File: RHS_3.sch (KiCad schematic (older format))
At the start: 64 parts, among them IC1 ATMEGA328P-A, IC2 CC1101, IC3 CC1101_Chip, J1 Glass Breakage Detector, J2 ANT, P4 ISP Bottom, P5 ISP Top, P6 FTDI, P7 ISP 10, SW1 Reset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

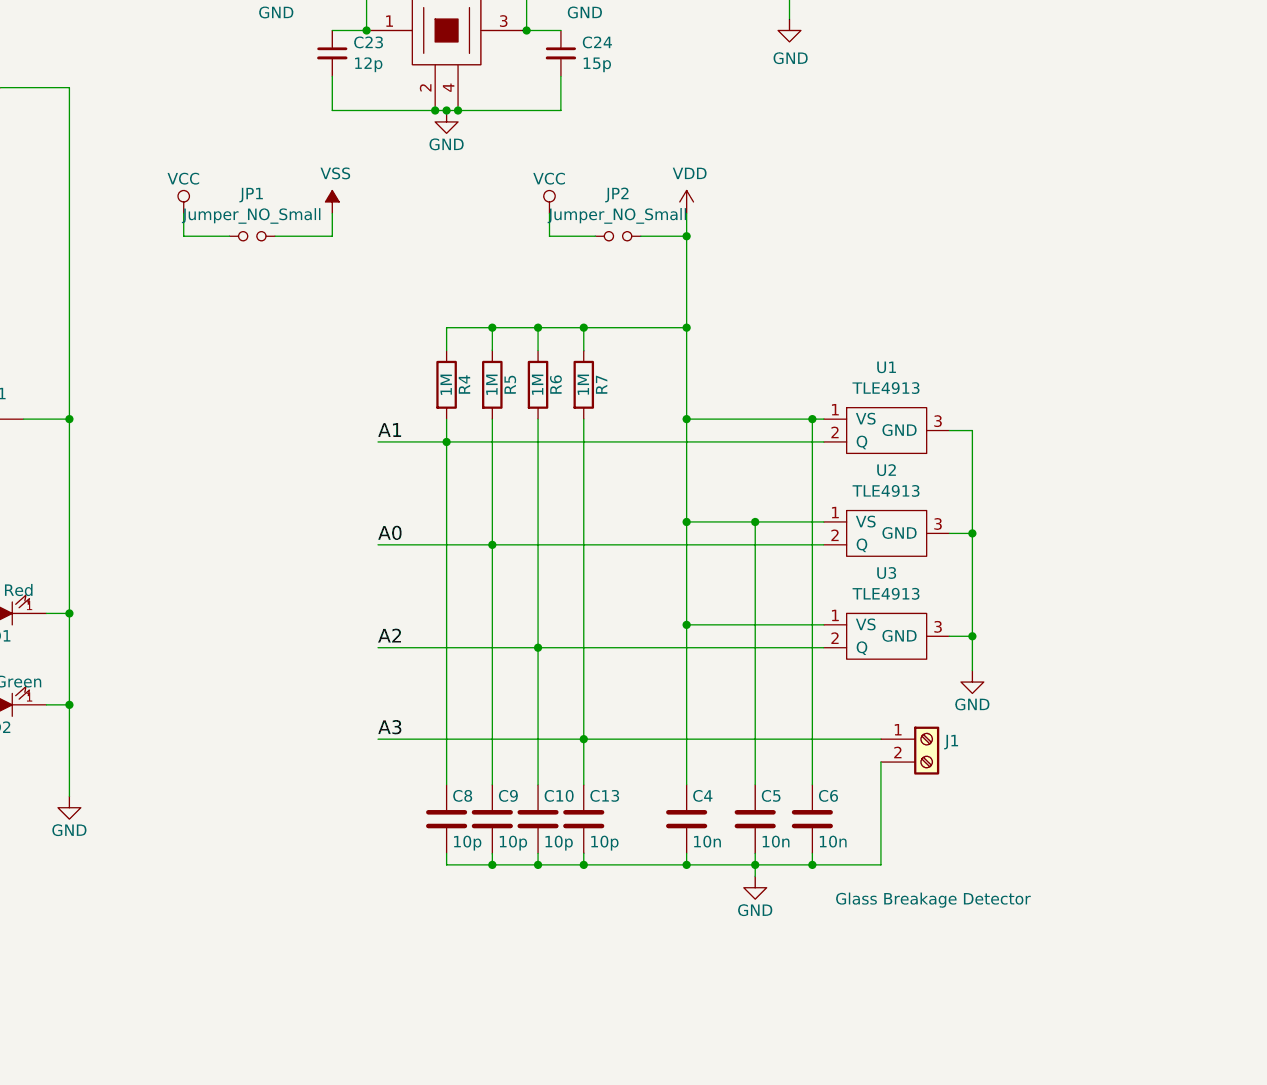
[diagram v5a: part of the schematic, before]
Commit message: layout changed
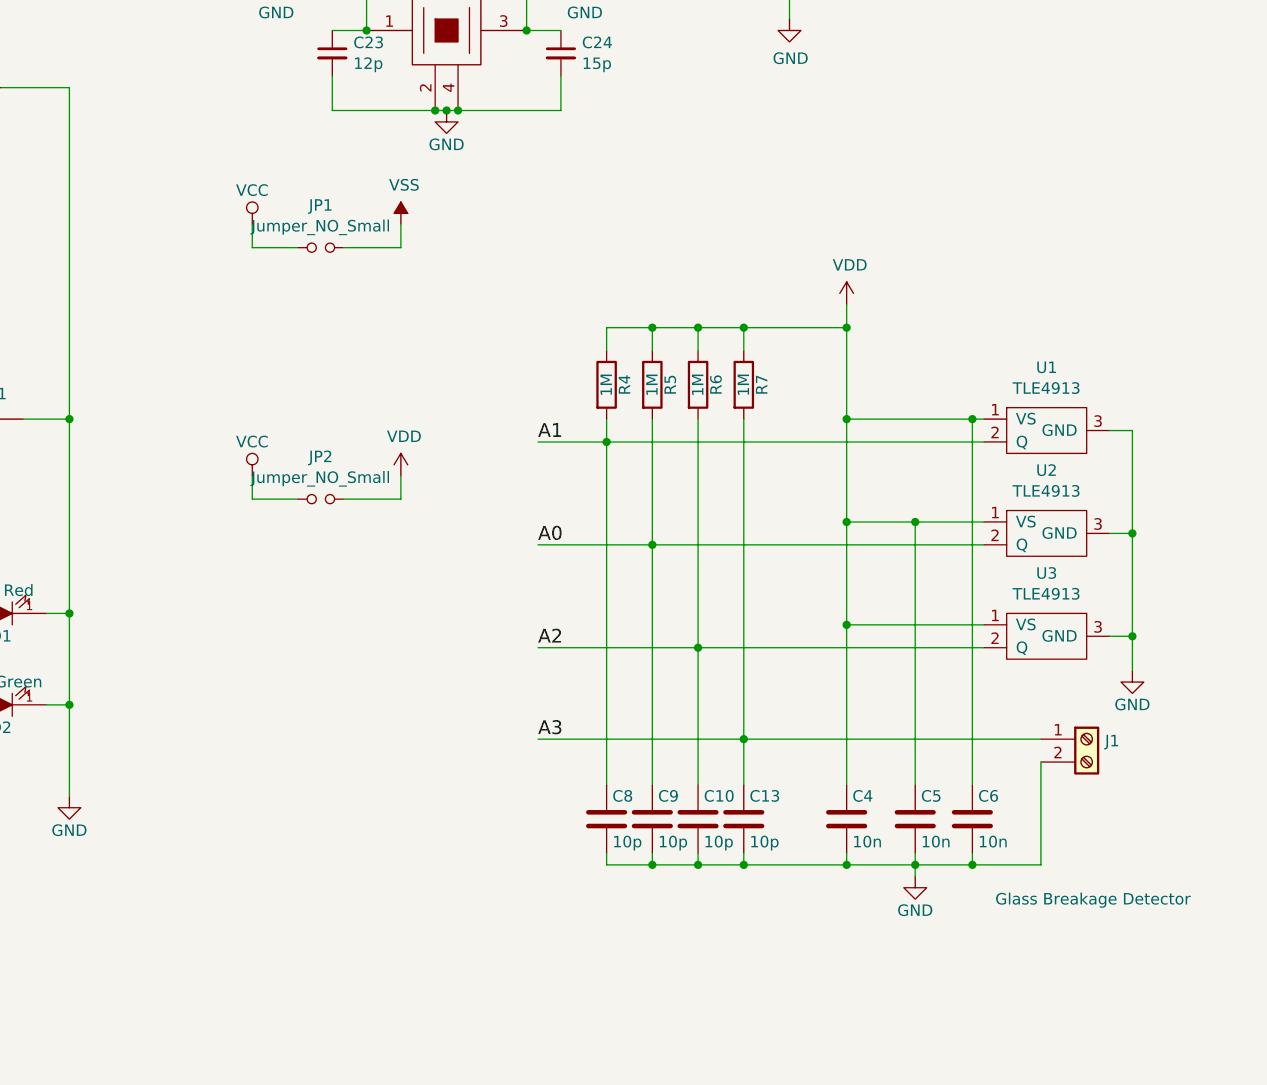
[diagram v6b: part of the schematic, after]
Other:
- moved on the sheet: C10, C13, C4, C5, C6, C8, C9, J1, JP1, JP2, R4, R5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

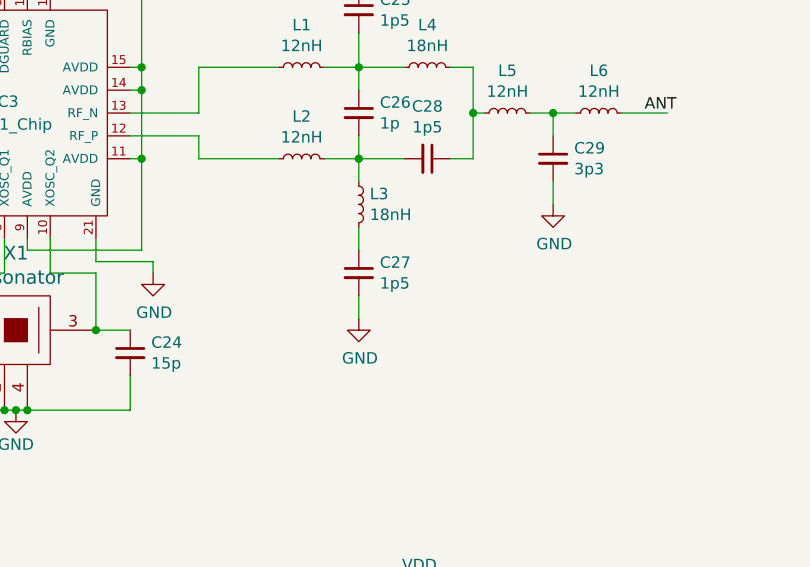
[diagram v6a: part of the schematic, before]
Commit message: part numbers added
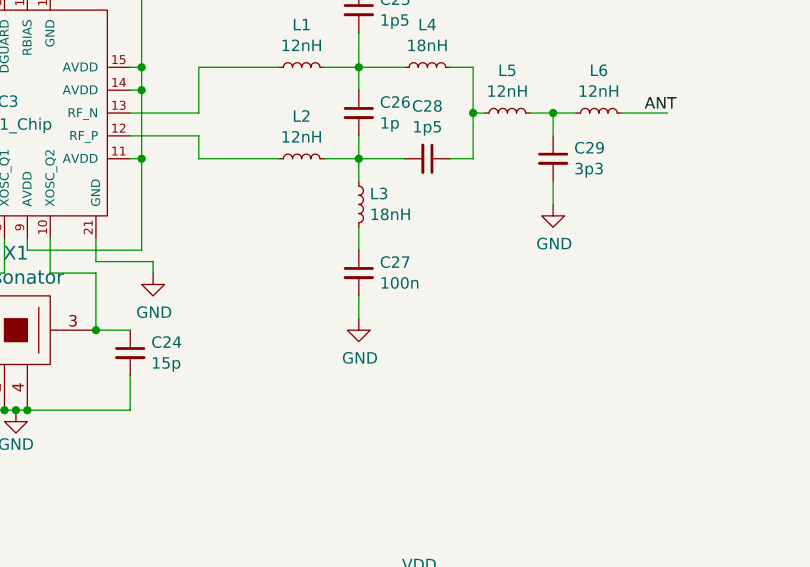
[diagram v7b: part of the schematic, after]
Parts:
- C15: LCSC Part # (none) -> C23733
- C16, C17, C18, C19, C20, C21, C22: LCSC Part # (none) -> C1525
- C23: LCSC Part # (none) -> C1547
- C24: LCSC Part # (none) -> C1548
- C25, C28: LCSC Part # (none) -> C1552
- C26: LCSC Part # (none) -> C1550
- C27: value 1p5 -> 100n; LCSC Part # (none) -> C1525
- C29: LCSC Part # (none) -> C1565
- IC3: LCSC Part # (none) -> C29953
- L1, L2, L5, L6: LCSC Part # (none) -> C24563
- L3, L4: LCSC Part # (none) -> C24562
- X1: LCSC Part # (none) -> C91747
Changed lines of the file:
@@
 F 2 "Package_DFN_QFN:QFN-20-1EP_4x4mm_P0.5mm_EP2.5x2.5mm" H 7850 1650 50  0001 C CNN
 F 3 "" H 7850 1650 50  0001 C CNN
+F 4 "C29953" H 7850 1650 50  0001 C CNN "LCSC Part #"
 	1    7850 1650
 	1    0    0    -1
@@
 F 2 "Oscillator:Oscillator_SMD_EuroQuartz_XO32-4Pin_3.2x2.5mm" H 7900 2831 60  0001 C CNN
 F 3 "" H 7900 2550 60  0000 C CNN
+F 4 "C91747" H 7900 2600 50  0001 C CNN "LCSC Part #"
 	1    7900 2600
 	1    0    0    -1
@@
 F 2 "Capacitor_SMD:C_0402_1005Metric" H 7400 2700 50  0001 C CNN
 F 3 "~" H 7400 2700 50  0001 C CNN
+F 4 "C1547" H 7400 2700 50  0001 C CNN "LCSC Part #"
 	1    7400 2700
 	1    0    0    -1
@@
 F 2 "Capacitor_SMD:C_0402_1005Metric" H 8400 2700 50  0001 C CNN
 F 3 "~" H 8400 2700 50  0001 C CNN
+F 4 "C1548" H 8400 2700 50  0001 C CNN "LCSC Part #"
 	1    8400 2700
 	1    0    0    -1
@@
 F 2 "Capacitor_SMD:C_0402_1005Metric" H 7150 2050 50  0001 C CNN
 F 3 "~" H 7150 2050 50  0001 C CNN
+F 4 "C1525" H 7150 2050 50  0001 C CNN "LCSC Part #"
 	1    7150 2050
 	1    0    0    -1
@@
 F 2 "Inductor_SMD:L_0402_1005Metric" H 9150 1450 50  0001 C CNN
 F 3 "~" H 9150 1450 50  0001 C CNN
+F 4 "C24563" H 9150 1450 50  0001 C CNN "LCSC Part #"
 	1    9150 1450
 	0    -1   -1   0
@@
 F 2 "Inductor_SMD:L_0402_1005Metric" H 9150 1850 50  0001 C CNN
 F 3 "~" H 9150 1850 50  0001 C CNN
+F 4 "C24563" H 9150 1850 50  0001 C CNN "LCSC Part #"
 	1    9150 1850
 	0    -1   -1   0
@@
 F 2 "Capacitor_SMD:C_0402_1005Metric" H 9400 1650 50  0001 C CNN
 F 3 "~" H 9400 1650 50  0001 C CNN
+F 4 "C1550" H 9400 1650 50  0001 C CNN "LCSC Part #"
 	1    9400 1650
 	1    0    0    -1
@@
 F 2 "Capacitor_SMD:C_0402_1005Metric" H 9400 1200 50  0001 C CNN
 F 3 "~" H 9400 1200 50  0001 C CNN
+F 4 "C1552" H 9400 1200 50  0001 C CNN "LCSC Part #"
 	1    9400 1200
 	1    0    0    -1
@@
 F 2 "Inductor_SMD:L_0402_1005Metric" H 9400 2050 50  0001 C CNN
 F 3 "~" H 9400 2050 50  0001 C CNN
+F 4 "C24562" H 9400 2050 50  0001 C CNN "LCSC Part #"
 	1    9400 2050
 	1    0    0    -1
@@
 F 2 "Inductor_SMD:L_0402_1005Metric" H 9700 1450 50  0001 C CNN
 F 3 "~" H 9700 1450 50  0001 C CNN
+F 4 "C24562" H 9700 1450 50  0001 C CNN "LCSC Part #"
 	1    9700 1450
 	0    -1   -1   0
@@
 F 2 "Capacitor_SMD:C_0402_1005Metric" H 9700 1850 50  0001 C CNN
 F 3 "~" H 9700 1850 50  0001 C CNN
+F 4 "C1552" H 9700 1850 50  0001 C CNN "LCSC Part #"
 	1    9700 1850
 	0    1    1    0
@@
 F 2 "Inductor_SMD:L_0402_1005Metric" H 10050 1650 50  0001 C CNN
 F 3 "~" H 10050 1650 50  0001 C CNN
+F 4 "C24563" H 10050 1650 50  0001 C CNN "LCSC Part #"
 	1    10050 1650
 	0    -1   -1   0
@@
 F 2 "Inductor_SMD:L_0402_1005Metric" H 10450 1650 50  0001 C CNN
 F 3 "~" H 10450 1650 50  0001 C CNN
+F 4 "C24563" H 10450 1650 50  0001 C CNN "LCSC Part #"
 	1    10450 1650
 	0    -1   -1   0
@@
 F 2 "Capacitor_SMD:C_0402_1005Metric" H 10250 1850 50  0001 C CNN
 F 3 "~" H 10250 1850 50  0001 C CNN
+F 4 "C1565" H 10250 1850 50  0001 C CNN "LCSC Part #"
 	1    10250 1850
 	1    0    0    -1
@@
 P 9400 2350
 F 0 "C27" H 9492 2396 50  0000 L CNN
-F 1 "1p5" H 9492 2305 50  0000 L CNN
+F 1 "100n" H 9492 2305 50  0000 L CNN
 F 2 "Capacitor_SMD:C_0402_1005Metric" H 9400 2350 50  0001 C CNN
 F 3 "~" H 9400 2350 50  0001 C CNN
+F 4 "C1525" H 9400 2350 50  0001 C CNN "LCSC Part #"
 	1    9400 2350
 	1    0    0    -1
@@
 F 2 "Capacitor_SMD:C_0402_1005Metric" H 6600 1000 50  0001 C CNN
 F 3 "~" H 6600 1000 50  0001 C CNN
+F 4 "C1525" H 6600 1000 50  0001 C CNN "LCSC Part #"
 	1    6600 1000
 	1    0    0    -1
@@
 F 2 "Capacitor_SMD:C_0402_1005Metric" H 6350 1000 50  0001 C CNN
 F 3 "~" H 6350 1000 50  0001 C CNN
+F 4 "C1525" H 6350 1000 50  0001 C CNN "LCSC Part #"
 	1    6350 1000
 	1    0    0    -1
@@
 F 2 "Capacitor_SMD:C_0402_1005Metric" H 6050 1000 50  0001 C CNN
 F 3 "~" H 6050 1000 50  0001 C CNN
+F 4 "C1525" H 6050 1000 50  0001 C CNN "LCSC Part #"
 	1    6050 1000
 	1    0    0    -1
@@
 F 2 "Capacitor_SMD:C_0402_1005Metric" H 5750 1000 50  0001 C CNN
 F 3 "~" H 5750 1000 50  0001 C CNN
+F 4 "C1525" H 5750 1000 50  0001 C CNN "LCSC Part #"
 	1    5750 1000
 	1    0    0    -1
@@
 F 2 "Capacitor_SMD:C_0402_1005Metric" H 5450 1000 50  0001 C CNN
 F 3 "~" H 5450 1000 50  0001 C CNN
+F 4 "C1525" H 5450 1000 50  0001 C CNN "LCSC Part #"
 	1    5450 1000
 	1    0    0    -1
@@
 F 2 "Capacitor_SMD:C_0402_1005Metric" H 5150 1000 50  0001 C CNN
 F 3 "~" H 5150 1000 50  0001 C CNN
+F 4 "C1525" H 5150 1000 50  0001 C CNN "LCSC Part #"
 	1    5150 1000
 	1    0    0    -1
@@
 F 2 "Capacitor_SMD:C_0402_1005Metric" H 4850 1000 50  0001 C CNN
 F 3 "~" H 4850 1000 50  0001 C CNN
+F 4 "C23733" H 4850 1000 50  0001 C CNN "LCSC Part #"
 	1    4850 1000
 	1    0    0    -1
